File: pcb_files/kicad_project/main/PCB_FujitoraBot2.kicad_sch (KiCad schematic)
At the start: 99 parts, among them IC1 AS5040, IC2 AS5040, J1 MORRO1, SW2 SW_Reset, SW4 SW_Push, U2 LM1117MP-3.3, U3 MPU-6500, Y1 Crystal_GND24

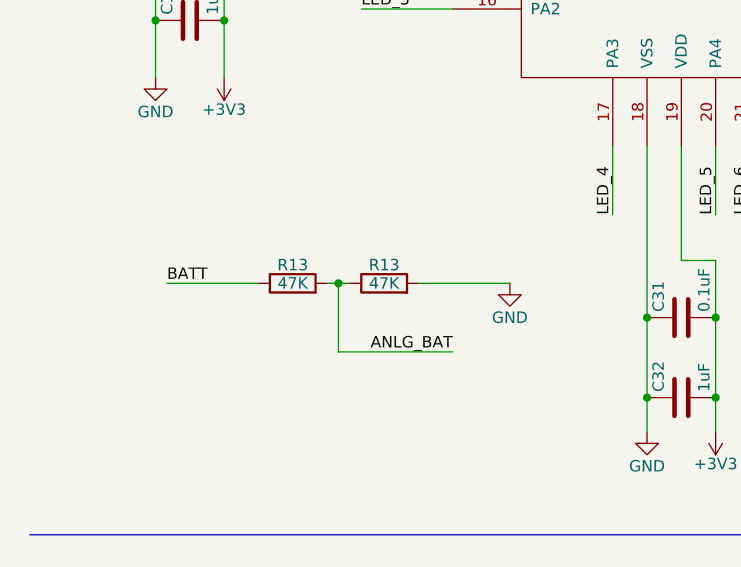
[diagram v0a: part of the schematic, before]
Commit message: Continua la puesta en marcha de Fujitora comprobando que todo funcione individualmente
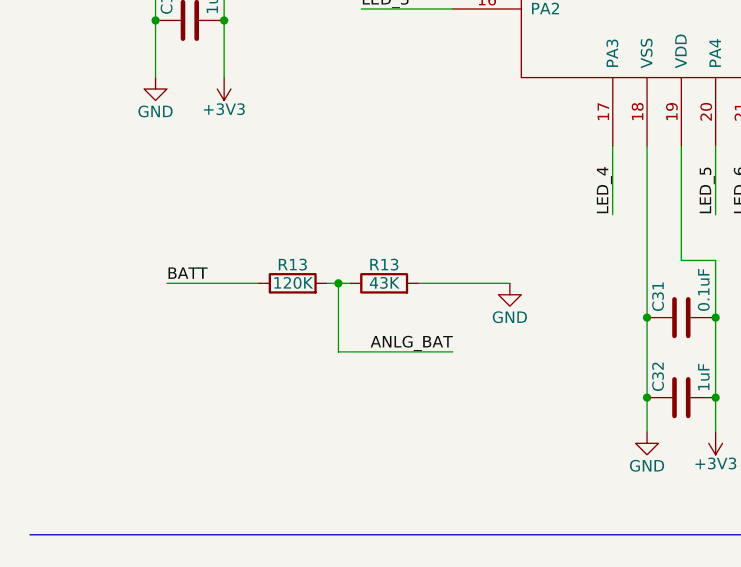
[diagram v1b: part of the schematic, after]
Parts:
- R13: value 47K -> 120K
- R13: value 47K -> 43K
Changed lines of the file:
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@@
 			)
 		)
-		(property "Value" "47K"
+		(property "Value" "120K"
 			(at 43.18 144.78 90)
 			(effects
@@
 			)
 		)
-		(property "Value" "47K"
+		(property "Value" "43K"
 			(at 53.34 144.78 90)
 			(effects
